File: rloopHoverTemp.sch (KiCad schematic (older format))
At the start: 22 parts, among them P1 CONN_01X01, P2 CONN_01X01, P3 CONN_01X01, P4 CONN_01X01, U1 P82B715TD, U2 MLX90614, U3 Regulator, U4 Regulator, X1 CONN_01X05

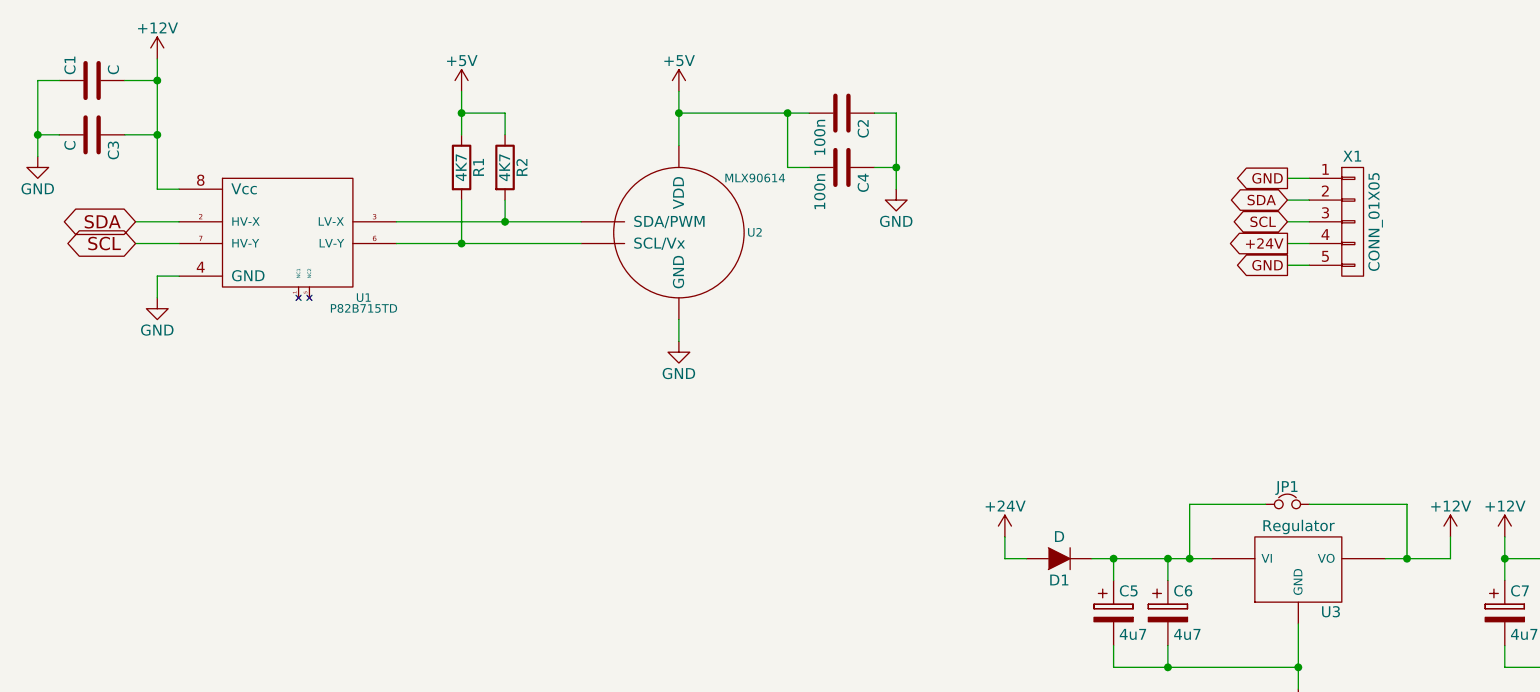
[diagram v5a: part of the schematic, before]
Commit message: dual MNL connector version
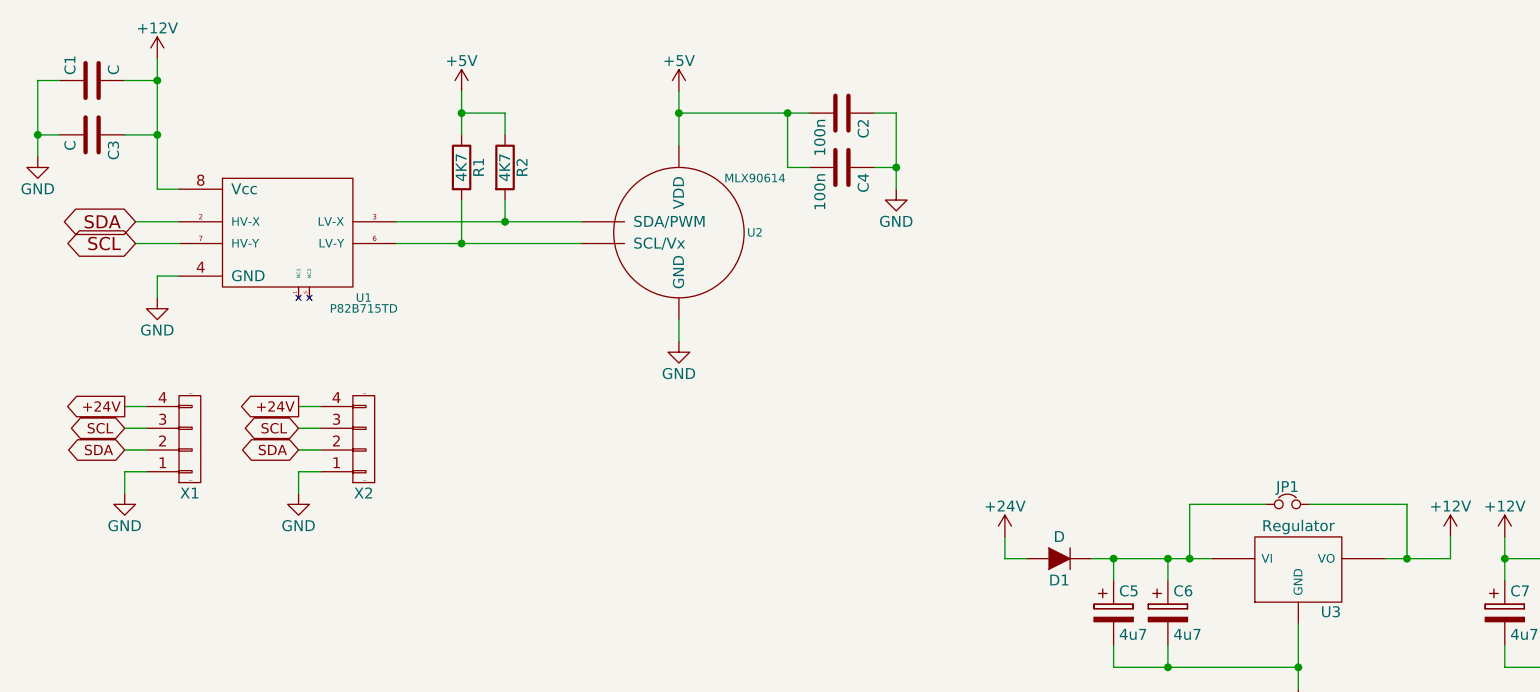
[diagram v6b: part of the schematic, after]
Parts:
- removed X1: CONN_01X05, Pin_Headers:Pin_Header_Angled_1x05, symbol CONN_01X05
- added X1, X2: CONN_01X04-2XMNT, -footprints:CONN-TE-MICROMNL-4-PTH-MALE-RGT, symbol CONN_01X04-2XMNT
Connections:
- net +24V: now also X1.4 (P4), X2.4 (P4)
- net GND: now also X1.1 (P1), X1.M1, X1.M2, X2.1 (P1), X2.M1, X2.M2
- net SCL: now also X1.3 (P3), X2.3 (P3)
- net SDA: now also X1.2 (P2), X2.2 (P2)
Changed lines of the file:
@@
 LIBS:valves
 LIBS:rloop
+LIBS:rloopHoverTemp-cache
 EELAYER 25 0
 EELAYER END
@@
 Text GLabel 2200 1700 0    60   BiDi ~ 0
 SCL
-$Comp
-L CONN_01X05 X1
-U 1 1 57405195
-P 7800 1600
-F 0 "X1" H 7800 1900 50  0000 C CNN
-F 1 "CONN_01X05" V 7900 1600 50  0000 C CNN
-F 2 "Pin_Headers:Pin_Header_Angled_1x05" H 7800 1600 50  0001 C CNN
-F 3 "" H 7800 1600 50  0000 C CNN
-	1    7800 1600
-	1    0    0    -1
-$EndComp
-Wire Wire Line
-	7600 1600 7500 1600
-Wire Wire Line
-	7600 1800 7500 1800
-Wire Wire Line
-	7600 1400 7500 1400
-Text GLabel 7500 1800 0    47   Output ~ 0
+Text GLabel 2150 2450 0    47   Output ~ 0
++24V
+$Comp
+L CONN_01X04-2XMNT X1
+U 1 1 5740FB83
+P 2450 2600
+F 0 "X1" H 2450 2850 50  0000 C CNN
+F 1 "CONN_01X04-2XMNT" V 2550 2600 50  0001 C CNN
+F 2 "-footprints:CONN-TE-MICROMNL-4-PTH-MALE-RGT" H 2450 2600 50  0001 C CNN
+F 3 "" H 2450 2600 50  0000 C CNN
+	1    2450 2600
+	1    0    0    1
+$EndComp
+Text GLabel 2150 2650 0    47   BiDi ~ 0
+SDA
+Text GLabel 2150 2550 0    47   BiDi ~ 0
+SCL
+$Comp
+L GND #PWR014
+U 1 1 574107FA
+P 2150 2850
+F 0 "#PWR014" H 2150 2600 50  0001 C CNN
+F 1 "GND" H 2150 2700 50  0000 C CNN
+F 2 "" H 2150 2850 50  0000 C CNN
+F 3 "" H 2150 2850 50  0000 C CNN
+	1    2150 2850
+	1    0    0    -1
+$EndComp
+Wire Wire Line
+	2250 2750 2150 2750
+Wire Wire Line
+	2150 2750 2150 2850
+Wire Wire Line
+	2250 2650 2150 2650
+Wire Wire Line
+	2250 2550 2150 2550
+Wire Wire Line
+	2250 2450 2150 2450
+Text Label 2450 2800 0    4    ~ 0
 GND
-Text GLabel 7500 1400 0    47   Output ~ 0
+Text Label 2450 2400 0    4    ~ 0
 GND
-Text GLabel 7500 1700 0    47   Output ~ 0
+Text GLabel 2950 2450 0    47   Output ~ 0
 +24V
-Text GLabel 7500 1600 0    47   BiDi ~ 0
+$Comp
+L CONN_01X04-2XMNT X2
+U 1 1 57411842
+P 3250 2600
+F 0 "X2" H 3250 2850 50  0000 C CNN
+F 1 "CONN_01X04-2XMNT" V 3350 2600 50  0001 C CNN
+F 2 "-footprints:CONN-TE-MICROMNL-4-PTH-MALE-RGT" H 3250 2600 50  0001 C CNN
+F 3 "" H 3250 2600 50  0000 C CNN
+	1    3250 2600
+	1    0    0    1
+$EndComp
+Text GLabel 2950 2650 0    47   BiDi ~ 0
+SDA
+Text GLabel 2950 2550 0    47   BiDi ~ 0
 SCL
-Text GLabel 7500 1500 0    47   BiDi ~ 0
-SDA
-Wire Wire Line
-	7600 1500 7500 1500
-Wire Wire Line
-	7500 1700 7600 1700
+$Comp
+L GND #PWR?
+U 1 1 5741184A
+P 2950 2850
+F 0 "#PWR?" H 2950 2600 50  0001 C CNN
+F 1 "GND" H 2950 2700 50  0000 C CNN
+F 2 "" H 2950 2850 50  0000 C CNN
+F 3 "" H 2950 2850 50  0000 C CNN
+	1    2950 2850
+	1    0    0    -1
+$EndComp
+Wire Wire Line
+	3050 2750 2950 2750
+Wire Wire Line
+	2950 2750 2950 2850
+Wire Wire Line
+	3050 2650 2950 2650
+Wire Wire Line
+	3050 2550 2950 2550
+Wire Wire Line
+	3050 2450 2950 2450
+Text Label 3250 2800 0    4    ~ 0
+GND
+Text Label 3250 2400 0    4    ~ 0
+GND
 $EndSCHEMATC

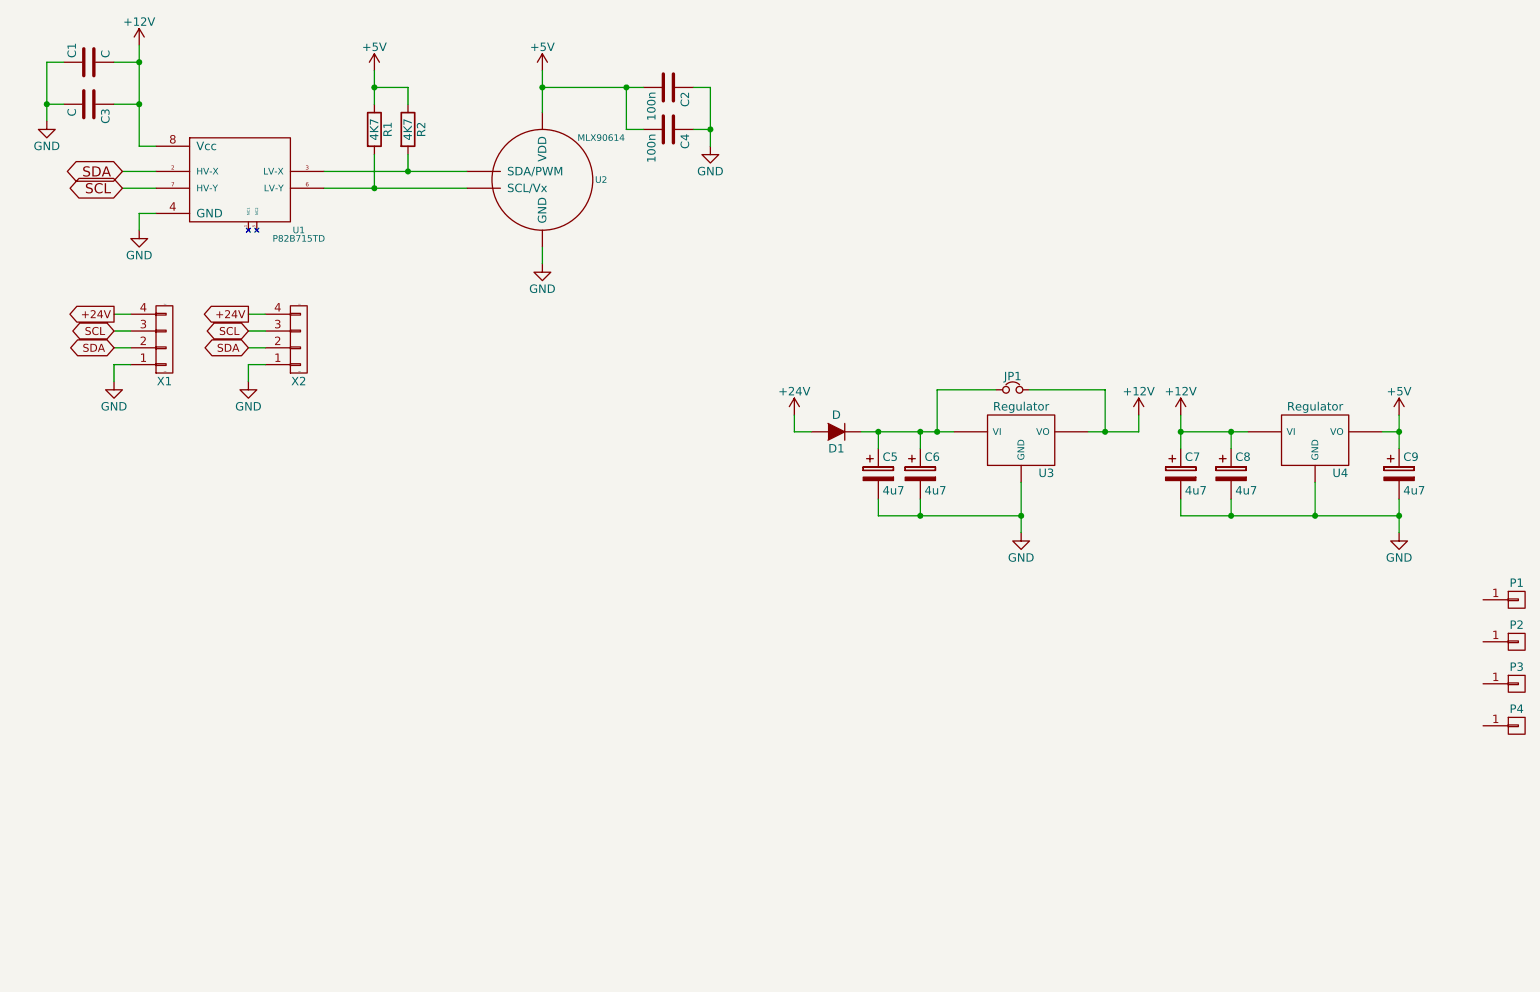
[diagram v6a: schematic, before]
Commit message: version with dual RJ45 connector
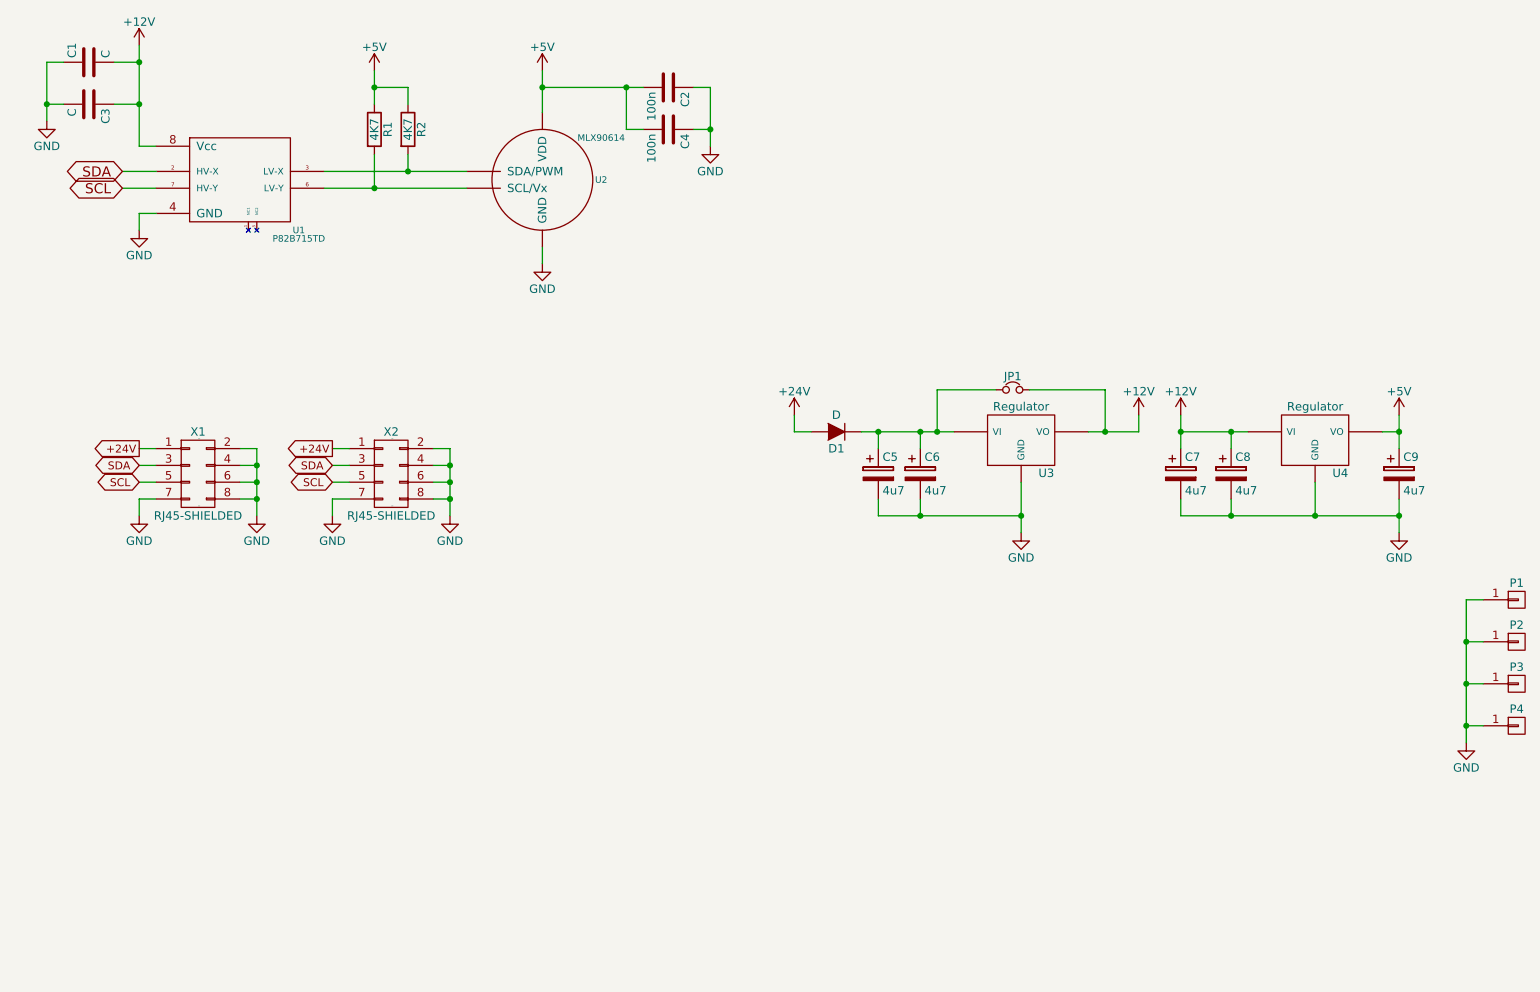
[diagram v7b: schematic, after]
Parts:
- removed X1, X2: CONN_01X04-2XMNT, -footprints:CONN-TE-MICROMNL-4-PTH-MALE-RGT, symbol CONN_01X04-2XMNT
- added X1, X2: RJ45-SHIELDED, -footprints:RJ45-TE-5558342-1, symbol RJ45-SHIELDED
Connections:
- net +24V: now also X1.1 (P1), X2.1 (P1)
- net GND: now also P1.1 (P1), P2.1 (P1), P3.1 (P1), P4.1 (P1), X1.2 (P2), X1.4 (P4), X1.6 (P6), X1.7 (P7), X1.8 (P8), X1.SHLD (SHLD2), X2.2 (P2), X2.4 (P4), X2.6 (P6), X2.7 (P7), X2.8 (P8), X2.SHLD (SHLD2)
- net SCL: now also X1.5 (P5), X2.5 (P5)
- net SDA: now also X1.3 (P3), X2.3 (P3)
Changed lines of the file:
@@
 Text GLabel 2200 1700 0    60   BiDi ~ 0
 SCL
-Text GLabel 2150 2450 0    47   Output ~ 0
+Text GLabel 2300 3250 0    47   Output ~ 0
 +24V
+Text Label 2650 3600 0    4    ~ 0
+GND
+Text Label 2650 3200 0    4    ~ 0
+GND
 $Comp
-L CONN_01X04-2XMNT X1
-U 1 1 5740FB83
-P 2450 2600
-F 0 "X1" H 2450 2850 50  0000 C CNN
-F 1 "CONN_01X04-2XMNT" V 2550 2600 50  0001 C CNN
-F 2 "-footprints:CONN-TE-MICROMNL-4-PTH-MALE-RGT" H 2450 2600 50  0001 C CNN
-F 3 "" H 2450 2600 50  0000 C CNN
-	1    2450 2600
-	1    0    0    1
+L RJ45-SHIELDED X1
+U 1 1 5741248E
+P 2650 3400
+F 0 "X1" H 2650 3650 50  0000 C CNN
+F 1 "RJ45-SHIELDED" H 2650 3150 50  0000 C CNN
+F 2 "-footprints:RJ45-TE-5558342-1" H 2650 2200 50  0001 C CNN
+F 3 "" H 2650 2200 50  0000 C CNN
+	1    2650 3400
+	1    0    0    -1
 $EndComp
-Text GLabel 2150 2650 0    47   BiDi ~ 0
+Text GLabel 2300 3350 0    47   BiDi ~ 0
 SDA
-Text GLabel 2150 2550 0    47   BiDi ~ 0
+Text GLabel 2300 3450 0    47   BiDi ~ 0
 SCL
+Wire Wire Line
+	2400 3450 2300 3450
+Wire Wire Line
+	2400 3350 2300 3350
+Wire Wire Line
+	2400 3250 2300 3250
 $Comp
 L GND #PWR014
-U 1 1 574107FA
-P 2150 2850
-F 0 "#PWR014" H 2150 2600 50  0001 C CNN
-F 1 "GND" H 2150 2700 50  0000 C CNN
-F 2 "" H 2150 2850 50  0000 C CNN
-F 3 "" H 2150 2850 50  0000 C CNN
-	1    2150 2850
+U 1 1 57413A80
+P 2300 3650
+F 0 "#PWR014" H 2300 3400 50  0001 C CNN
+F 1 "GND" H 2300 3500 50  0000 C CNN
+F 2 "" H 2300 3650 50  0000 C CNN
+F 3 "" H 2300 3650 50  0000 C CNN
+	1    2300 3650
 	1    0    0    -1
 $EndComp
 Wire Wire Line
-	2250 2750 2150 2750
+	2400 3550 2300 3550
 Wire Wire Line
-	2150 2750 2150 2850
+	2300 3550 2300 3650
+Text GLabel 3450 3250 0    47   Output ~ 0
++24V
+Text Label 3800 3600 0    4    ~ 0
+GND
+Text Label 3800 3200 0    4    ~ 0
+GND
+$Comp
+L RJ45-SHIELDED X2
+U 1 1 57413CB0
+P 3800 3400
+F 0 "X2" H 3800 3650 50  0000 C CNN
+F 1 "RJ45-SHIELDED" H 3800 3150 50  0000 C CNN
+F 2 "-footprints:RJ45-TE-5558342-1" H 3800 2200 50  0001 C CNN
+F 3 "" H 3800 2200 50  0000 C CNN
+	1    3800 3400
+	1    0    0    -1
+$EndComp
+Text GLabel 3450 3350 0    47   BiDi ~ 0
+SDA
+Text GLabel 3450 3450 0    47   BiDi ~ 0
+SCL
 Wire Wire Line
-	2250 2650 2150 2650
+	3550 3450 3450 3450
 Wire Wire Line
-	2250 2550 2150 2550
+	3550 3350 3450 3350
 Wire Wire Line
-	2250 2450 2150 2450
-Text Label 2450 2800 0    4    ~ 0
-GND
-Text Label 2450 2400 0    4    ~ 0
-GND
-Text GLabel 2950 2450 0    47   Output ~ 0
-+24V
+	3550 3250 3450 3250
 $Comp
-L CONN_01X04-2XMNT X2
-U 1 1 57411842
-P 3250 2600
-F 0 "X2" H 3250 2850 50  0000 C CNN
-F 1 "CONN_01X04-2XMNT" V 3350 2600 50  0001 C CNN
-F 2 "-footprints:CONN-TE-MICROMNL-4-PTH-MALE-RGT" H 3250 2600 50  0001 C CNN
-F 3 "" H 3250 2600 50  0000 C CNN
-	1    3250 2600
-	1    0    0    1
-$EndComp
-Text GLabel 2950 2650 0    47   BiDi ~ 0
-SDA
-Text GLabel 2950 2550 0    47   BiDi ~ 0
-SCL
-$Comp
-L GND #PWR?
-U 1 1 5741184A
-P 2950 2850
-F 0 "#PWR?" H 2950 2600 50  0001 C CNN
-F 1 "GND" H 2950 2700 50  0000 C CNN
-F 2 "" H 2950 2850 50  0000 C CNN
-F 3 "" H 2950 2850 50  0000 C CNN
-	1    2950 2850
+L GND #PWR015
+U 1 1 57413CBB
+P 3450 3650
+F 0 "#PWR015" H 3450 3400 50  0001 C CNN
+F 1 "GND" H 3450 3500 50  0000 C CNN
+F 2 "" H 3450 3650 50  0000 C CNN
+F 3 "" H 3450 3650 50  0000 C CNN
+	1    3450 3650
 	1    0    0    -1
 $EndComp
 Wire Wire Line
-	3050 2750 2950 2750
+	3550 3550 3450 3550
 Wire Wire Line
-	2950 2750 2950 2850
+	3450 3550 3450 3650
+$Comp
+L GND #PWR?
+U 1 1 574140D6
+P 3000 3650
+F 0 "#PWR?" H 3000 3400 50  0001 C CNN
+F 1 "GND" H 3000 3500 50  0000 C CNN
+F 2 "" H 3000 3650 50  0000 C CNN
+F 3 "" H 3000 3650 50  0000 C CNN
+	1    3000 3650
+	1    0    0    -1
+$EndComp
+$Comp
+L GND #PWR?
+U 1 1 574141DE
+P 4150 3650
+F 0 "#PWR?" H 4150 3400 50  0001 C CNN
+F 1 "GND" H 4150 3500 50  0000 C CNN
+F 2 "" H 4150 3650 50  0000 C CNN
+F 3 "" H 4150 3650 50  0000 C CNN
+	1    4150 3650
+	1    0    0    -1
+$EndComp
 Wire Wire Line
-	3050 2650 2950 2650
+	4150 3650 4150 3250
 Wire Wire Line
-	3050 2550 2950 2550
+	4150 3250 4050 3250
 Wire Wire Line
-	3050 2450 2950 2450
-Text Label 3250 2800 0    4    ~ 0
-GND
-Text Label 3250 2400 0    4    ~ 0
-GND
+	4050 3350 4150 3350
+Connection ~ 4150 3350
+Wire Wire Line
+	4050 3450 4150 3450
+Connection ~ 4150 3450
+Wire Wire Line
+	4050 3550 4150 3550
+Connection ~ 4150 3550
+Wire Wire Line
+	2900 3250 3000 3250
+Wire Wire Line
+	3000 3250 3000 3650
+Wire Wire Line
+	2900 3550 3000 3550
+Connection ~ 3000 3550
+Wire Wire Line
+	2900 3450 3000 3450
+Connection ~ 3000 3450
+Wire Wire Line
+	2900 3350 3000 3350
+Connection ~ 3000 3350
+$Comp
+L GND #PWR?
+U 1 1 5741470F
+P 10200 5000
+F 0 "#PWR?" H 10200 4750 50  0001 C CNN
+F 1 "GND" H 10200 4850 50  0000 C CNN
+F 2 "" H 10200 5000 50  0000 C CNN
+F 3 "" H 10200 5000 50  0000 C CNN
+	1    10200 5000
+	1    0    0    -1
+$EndComp
+Wire Wire Line
+	10300 4900 10200 4900
+Wire Wire Line
+	10200 4150 10200 5000
+Wire Wire Line
+	10300 4650 10200 4650
+Connection ~ 10200 4900
+Wire Wire Line
+	10300 4400 10200 4400
+Connection ~ 10200 4650
+Wire Wire Line
+	10300 4150 10200 4150
+Connection ~ 10200 4400
 $EndSCHEMATC
